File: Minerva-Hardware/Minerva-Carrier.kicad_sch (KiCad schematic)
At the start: 33 parts, among them J11 USB_C_Receptacle_USB2.0, U1 BQ25798

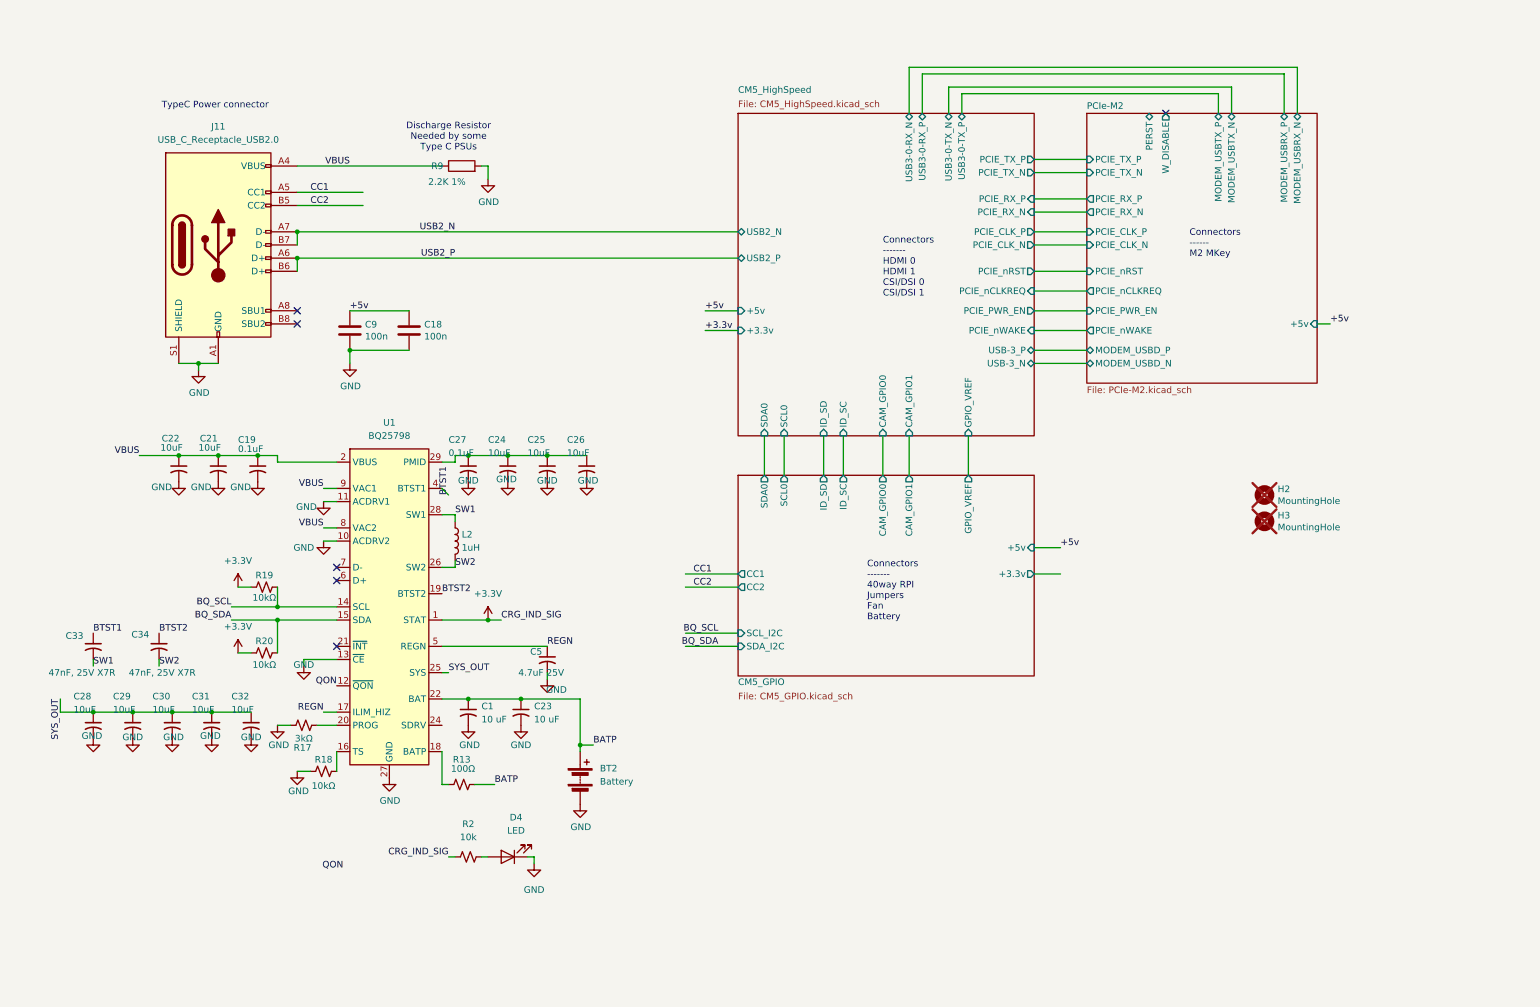
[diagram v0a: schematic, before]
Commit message: Capture pre-existing Minerva hardware and Torchform work
Hardware schematics and power architecture
- Update carrier, CM5 GPIO, high-speed, PCIe/M.2, face-board, and root schematic hierarchy.
- Add USB-C/DisplayPort dock path, PD controller support, display bridge, audio amplifier, battery charging, boost conversion, fuel gauge, RTC backup, and MCU interconnect changes.
- Add the relocated power/USB schematic and associated local symbols, footprints, and 3D models.

PCB and design assets
- Update the carrier PCB and project configuration.
- Add CM5, connector, power, battery, PD, and board-specific footprint libraries.
- Add the USB-C receptacle STEP model and supporting KiCad assets.
- Apply the surfaced carrier-board geometry cleanup and add the J23 shell-peg DRC rule.

Verification and reference material
- Add CM5 and component datasheets, extracted reference text, current netlist, DRC output, and hardware verification documentation.
- Update CONTEXT.md and workspace metadata with the current project state.

Torchform companion projects
- Add the standalone Qt/QML gamepad prototype.
- Add the Torchform QML GUI shell with screen, panel, radial-menu, keyboard, status, and startup components.
- Add the companion Rust input daemon prototype and configuration.

Project notes
- Add repository guidance and Minerva design/editor notes, including the power-usage note.
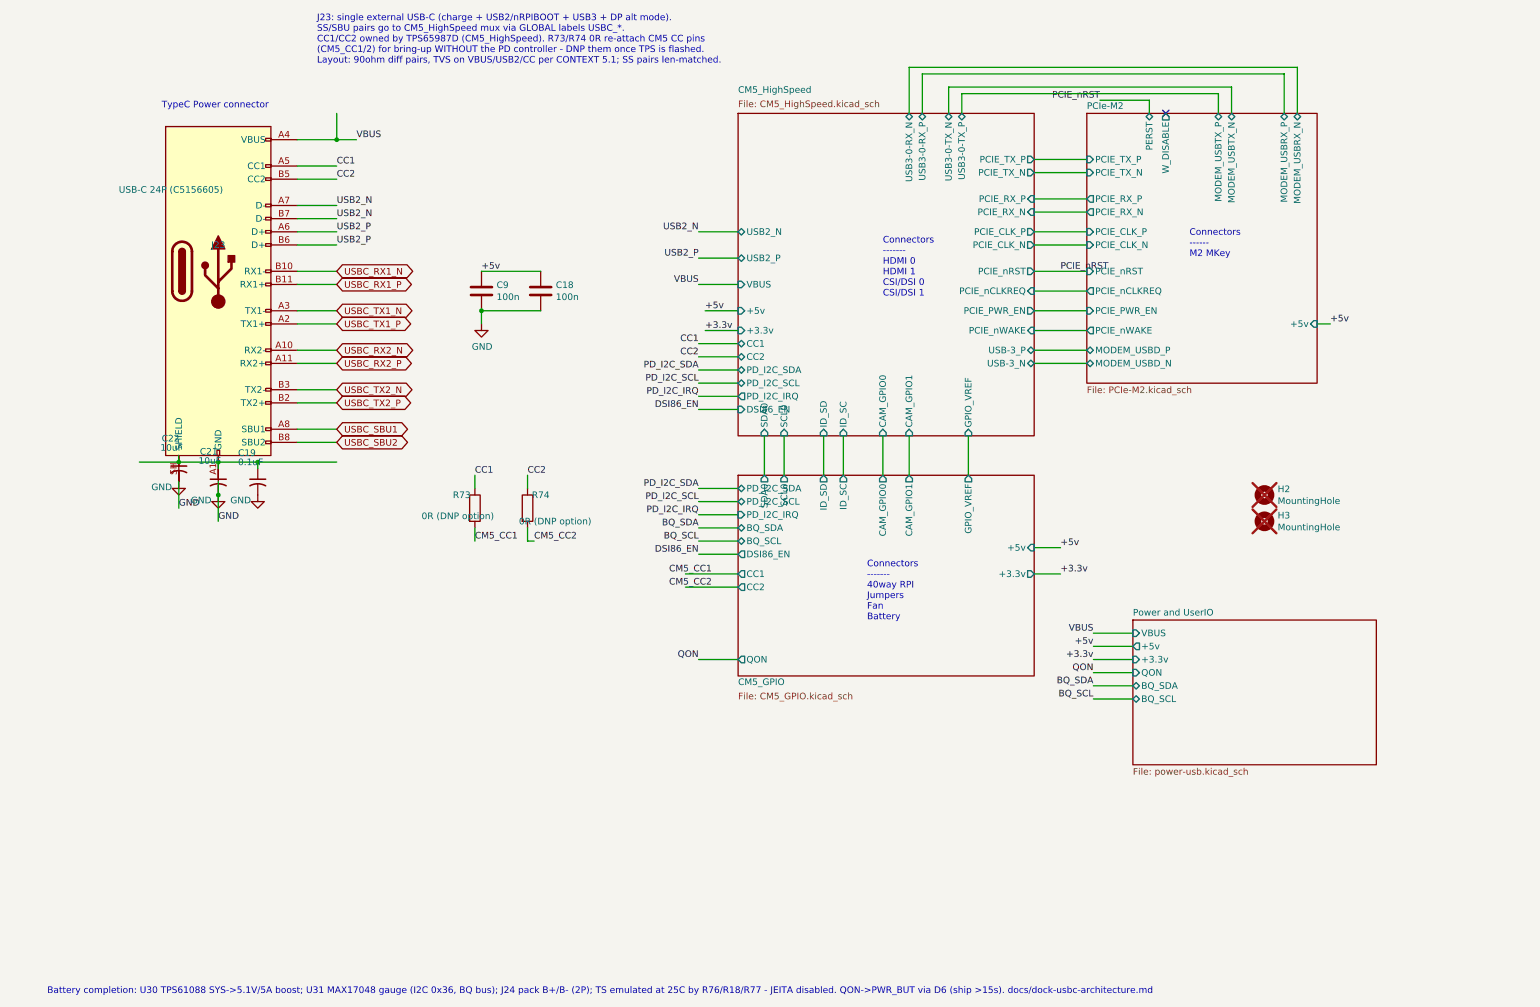
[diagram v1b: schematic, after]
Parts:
- removed BT2: Battery, Connector_JST:JST_ZE_S02B-ZESK-2D_1x02_P1.50mm_Horizontal, symbol Device:Battery
- removed C1, C23: 10 uF, Capacitor_SMD:C_0201_0603Metric, symbol Device:C_Small_US
- removed C24, C25, C26, C28, C29, C30, C31, C32: 10uF, Capacitor_SMD:C_01005_0402Metric, symbol Device:C_Small_US
- removed C27: 0.1uF, Capacitor_SMD:C_01005_0402Metric, symbol Device:C_Small_US
- removed C33, C34: 47nF, 25V X7R, Capacitor_SMD:C_01005_0402Metric, symbol Device:C_Small_US
- removed C5: 4.7uF 25V, Capacitor_SMD:C_0201_0603Metric, symbol Device:C_Small_US
- removed D4: LED, LED_SMD:LED_0201_0603Metric, symbol Device:LED
- removed J11: USB_C_Receptacle_USB2.0, Connector_USB:USB_C_Receptacle_GCT_USB4105-xx-A_16P_TopMnt_Horizontal, symbol Connector:USB_C_Receptacle_USB2.0_16P
- removed L2: 1uH, CM5 IO Board-rev2:L_Bourns_SRP5030CC, symbol Device:L
- removed R13: 100Ω, symbol Device:R_Small_US
- removed R17: 3kΩ, symbol Device:R_Small_US
- removed R18, R19, R20: 10kΩ, symbol Device:R_Small_US
- removed R2: 10k, Resistor_SMD:R_0201_0603Metric, symbol Device:R_Small_US
- removed R9: 2.2K 1%, Resistor_SMD:R_0402_1005Metric, symbol Device:R
- removed U1: BQ25798, Package_DFN_QFN:Texas_RQM0029A_VQFN-29_4x4mm_P0.4mm, symbol Battery_Management:BQ25798
- added J23: USB-C 24P (C5156605), Minerva:USBC_24P_QT143, symbol Connector:USB_C_Receptacle
- added R73, R74: 0R (DNP option), Resistor_SMD:R_0402_1005Metric, symbol Device:R
- H2, H3: footprint CM5IO:MountingHole_2.7mm_M2.5_DIN965 -> MountingHole:MountingHole_2.7mm_M2.5_DIN965
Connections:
- net CC1: now also J23.A5 (CC1), R73.1
- net CC2: now also J23.B5 (CC2), R74.1
- net GND: now also J23.A1 (GND), J23.A12 (GND), J23.B1 (GND), J23.B12 (GND), J23.SH (SHIELD)
- net USB2_N: now also J23.A7 (D-), J23.B7 (D-)
- net USB2_P: now also J23.A6 (D+), J23.B6 (D+)
- net VBUS: now also J23.A4 (VBUS), J23.A9 (VBUS), J23.B4 (VBUS), J23.B9 (VBUS); no longer C19.1, C21.1, C22.1
- new net: C19.1, C21.1, C22.1
- new net CM5_CC1: R73.2
- new net CM5_CC2: R74.2
- new net USBC_RX1_N: J23.B10 (RX1-)
- new net USBC_RX1_P: J23.B11 (RX1+)
- new net USBC_RX2_N: J23.A10 (RX2-)
- new net USBC_RX2_P: J23.A11 (RX2+)
- new net USBC_SBU1: J23.A8 (SBU1)
- new net USBC_SBU2: J23.B8 (SBU2)
- new net USBC_TX1_N: J23.A3 (TX1-)
- new net USBC_TX1_P: J23.A2 (TX1+)
- new net USBC_TX2_N: J23.B3 (TX2-)
- new net USBC_TX2_P: J23.B2 (TX2+)
- no-connect marks 6 -> 1
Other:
- added sheet Power and UserIO (power-usb.kicad_sch)
- sheet CM5_GPIO ports: added BQ_SCL, BQ_SDA, DSI86_EN, PD_I2C_IRQ, PD_I2C_SCL, PD_I2C_SDA, QON; removed SCL_I2C, SDA_I2C
- sheet CM5_HighSpeed ports: added CC1, CC2, DSI86_EN, PD_I2C_IRQ, PD_I2C_SCL, PD_I2C_SDA, VBUS; removed none
- note added: "Battery completion: U30 TPS61088 SYS->5.1V/5A boost; U31 MAX17048 gauge (I2C 0x36, BQ bus); J24 pack B+/B- (2P); TS emulated at 25C by R76/R18/R77 - JEITA disabled. QON->PWR_BUT via D6 (ship >15s). docs/dock-usbc-architecture.md"
- note added: "J23: single external USB-C (charge + USB2/nRPIBOOT + USB3 + DP alt mode). SS/SBU pairs go to CM5_HighSpeed mux via GLOBAL labels USBC_*. CC1/CC2 owned by TPS65987D (CM5_HighSpeed). R73/R74 0R re-attach CM5 CC pins (CM5_CC1/2) for bring-up WITHOUT the PD controller - DNP them once TPS is flashed. Layout: 90ohm diff pairs, TVS on VBUS/USB2/CC per CONTEXT 5.1; SS pairs len-matched."
- note removed: "Discharge Resistor Needed by some Type C PSUs"
- moved on the sheet: C18, C19, C21, C9

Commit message: hardware: snapshot carrier and face-board integration
Hardware schematics and power:
- complete the BQ25798 charger, TPS61088 5 V boost, MAX17048 gauge, battery controls, and cross-sheet power hierarchy
- add the SN65DSI86 display bridge, HD3SS460 mux, TPS65987D PD controller, USB-C protection, M.2 support, and corrected named-interface wiring
- move the Core2350B0 onto the face-board interconnect, route controls through J25/J2, and make Select directly assert nRPIBOOT
- remove the obsolete J6/J8 expansion headers and move J23 USB-C to the carrier top-left with its VBUS switch and charger support cluster

PCB, footprints, and mechanical assets:
- establish the six-layer controlled-impedance carrier stack, net classes, HDI rules, ground/power planes, keepouts, and placed carrier floorplan
- add the routed two-layer Minerva-Face board with eleven controls, four M2.5 holes, interconnects, fiducials, and a 3.5-inch display datum
- add corrected project-local footprints and STEP models for Core2350B0, USB-C, bridge/PD/power ICs, PicoBlade connectors, M.2 hardware, and critical mechanical envelopes
- correct BAT54 pin mapping, TPS61088 thermal-via numbering, J23 shell geometry, and board-edge lug rules

Verification and reference material:
- add sourcing evidence, ERC/DRC artifacts, STEP assemblies, face render, mechanical coordinates, controlled-impedance notes, and strict connectivity checklists
- document the dock architecture and current board-to-board pin contract
- remove transient root-level DRC and netlist dumps

Torchform and workstation integration:
- fix four-column home navigation and add controller focus/adjustment for quick-settings volume and brightness sliders
- configure Kitty as the terminal backend and add the Minerva SSH workspace folder

Known work-in-progress at this snapshot:
- carrier schematic/PCB parity is clean, but routing remains incomplete at 499 unconnected items with 53 differential-pair tuning violations
- the face board is DRC-clean and f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
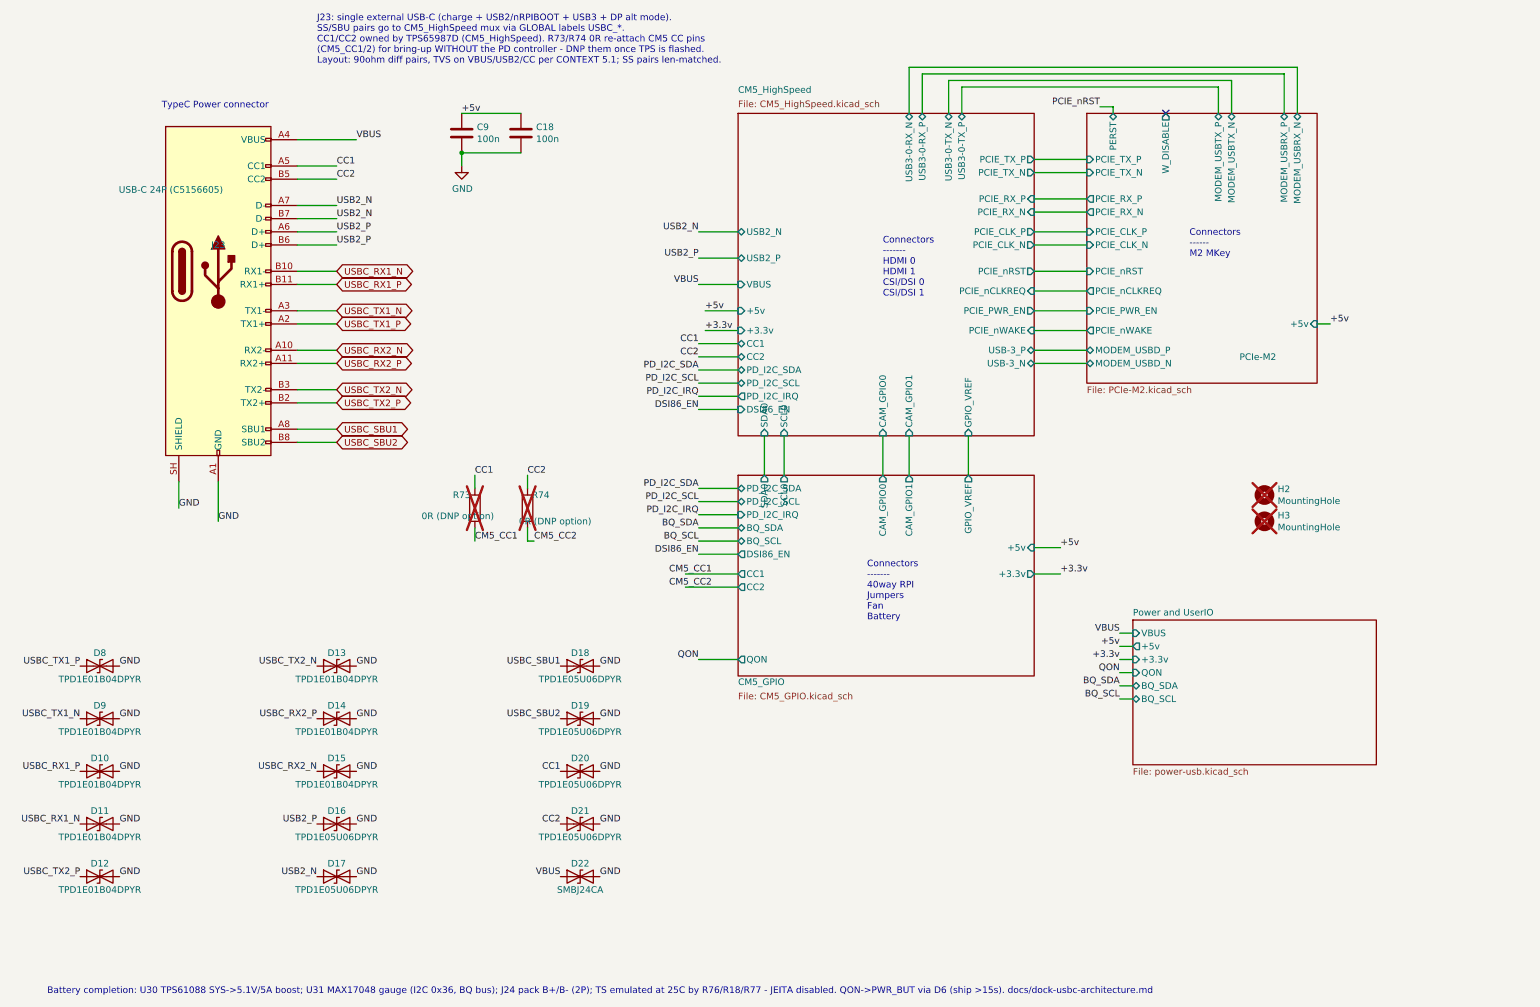
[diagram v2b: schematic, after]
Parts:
- removed C19: 0.1uF, Capacitor_SMD:C_01005_0402Metric, symbol Device:C_Small_US
- removed C21, C22: 10uF, Capacitor_SMD:C_01005_0402Metric, symbol Device:C_Small_US
- added D10, D11, D12, D13, D14, D15, D8, D9: TPD1E01B04DPYR, Package_SON:Texas_DPY0002A_0.6x1mm_P0.65mm, symbol Device:D_TVS
- added D16, D17, D18, D19, D20, D21: TPD1E05U06DPYR, Package_SON:Texas_DPY0002A_0.6x1mm_P0.65mm, symbol Device:D_TVS
- added D22: SMBJ24CA, Diode_SMD:D_SMB, symbol Device:D_TVS
- C18, C9: MPN (none) -> EMK105B7104KV-F; Manufacturer (none) -> Taiyo Yuden
- H2, H3: MPN (none) -> N/A; Manufacturer (none) -> PCB fabrication; Procurement Note (none) -> PCB feature; not purchased or placed
- J23: footprint Minerva:USBC_24P_QT143 -> Connector_USB:USB_C_Receptacle_Amphenol_12401610E4-2A_CircularHoles; MPN (none) -> QT143; Manufacturer (none) -> SHOU HAN; Procurement Note (none) -> LCSC C5156605
- R73, R74: MPN (none) -> RC0402JR-070RL; Manufacturer (none) -> Yageo; Procurement Note (none) -> DNP option; now not fitted
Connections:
- net CC1: now also D20.1 (A1)
- net CC2: now also D21.1 (A1)
- net GND: now also D10.2 (A2), D11.2 (A2), D12.2 (A2), D13.2 (A2), D14.2 (A2), D15.2 (A2), D16.2 (A2), D17.2 (A2), D18.2 (A2), D19.2 (A2), D20.2 (A2), D21.2 (A2), D22.2 (A2), D8.2 (A2), D9.2 (A2)
- net USB2_N: now also D17.1 (A1)
- net USB2_P: now also D16.1 (A1)
- net USBC_RX1_N: now also D11.1 (A1)
- net USBC_RX1_P: now also D10.1 (A1)
- net USBC_RX2_N: now also D15.1 (A1)
- net USBC_RX2_P: now also D14.1 (A1)
- net USBC_SBU1: now also D18.1 (A1)
- net USBC_SBU2: now also D19.1 (A1)
- net USBC_TX1_N: now also D9.1 (A1)
- net USBC_TX1_P: now also D8.1 (A1)
- net USBC_TX2_N: now also D13.1 (A1)
- net USBC_TX2_P: now also D12.1 (A1)
- net VBUS: now also D22.1 (A1)
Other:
- sheet CM5_GPIO ports: added none; removed ID_SC, ID_SD
- sheet CM5_HighSpeed ports: added none; removed ID_SC, ID_SD
- moved on the sheet: C18, C9
